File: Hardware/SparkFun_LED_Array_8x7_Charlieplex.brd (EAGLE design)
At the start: 27.9 x 43.2 mm, 73 parts

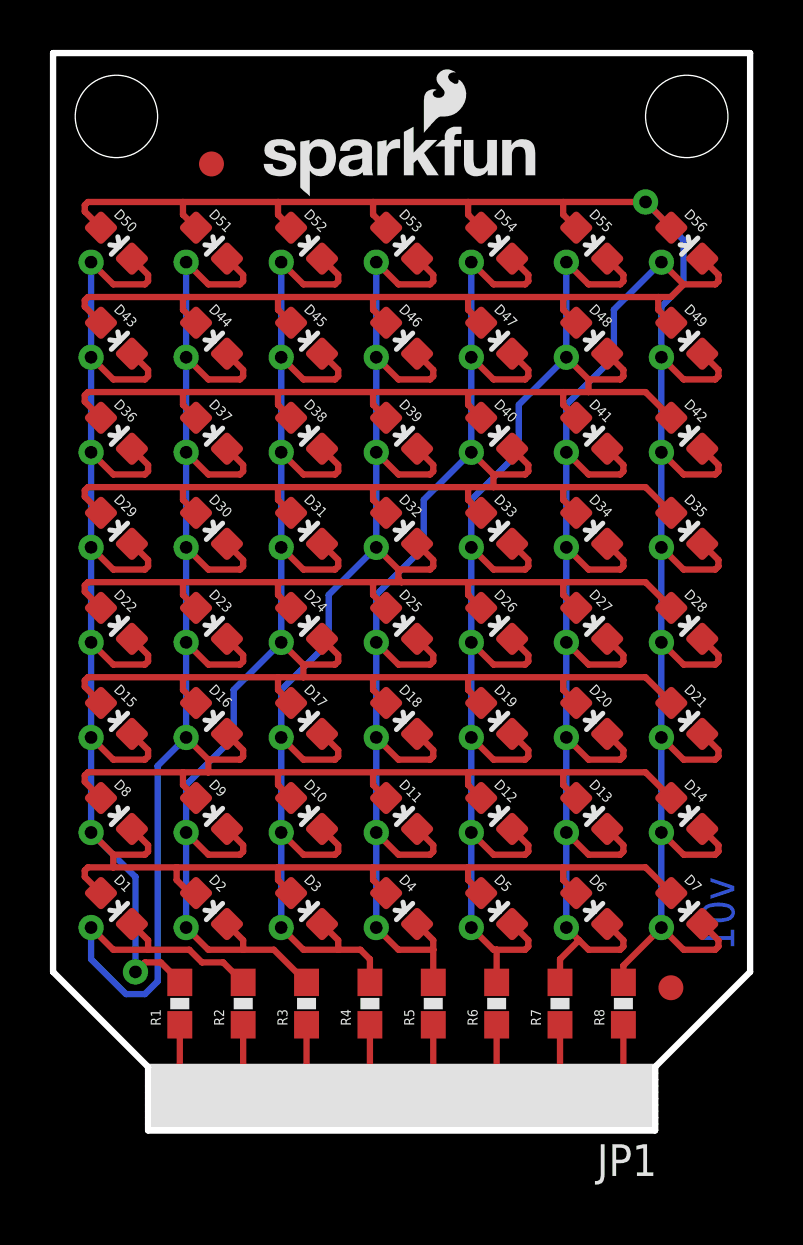
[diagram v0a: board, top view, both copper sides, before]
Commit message: Added BadgerHack logo. Moved some vias to make room.
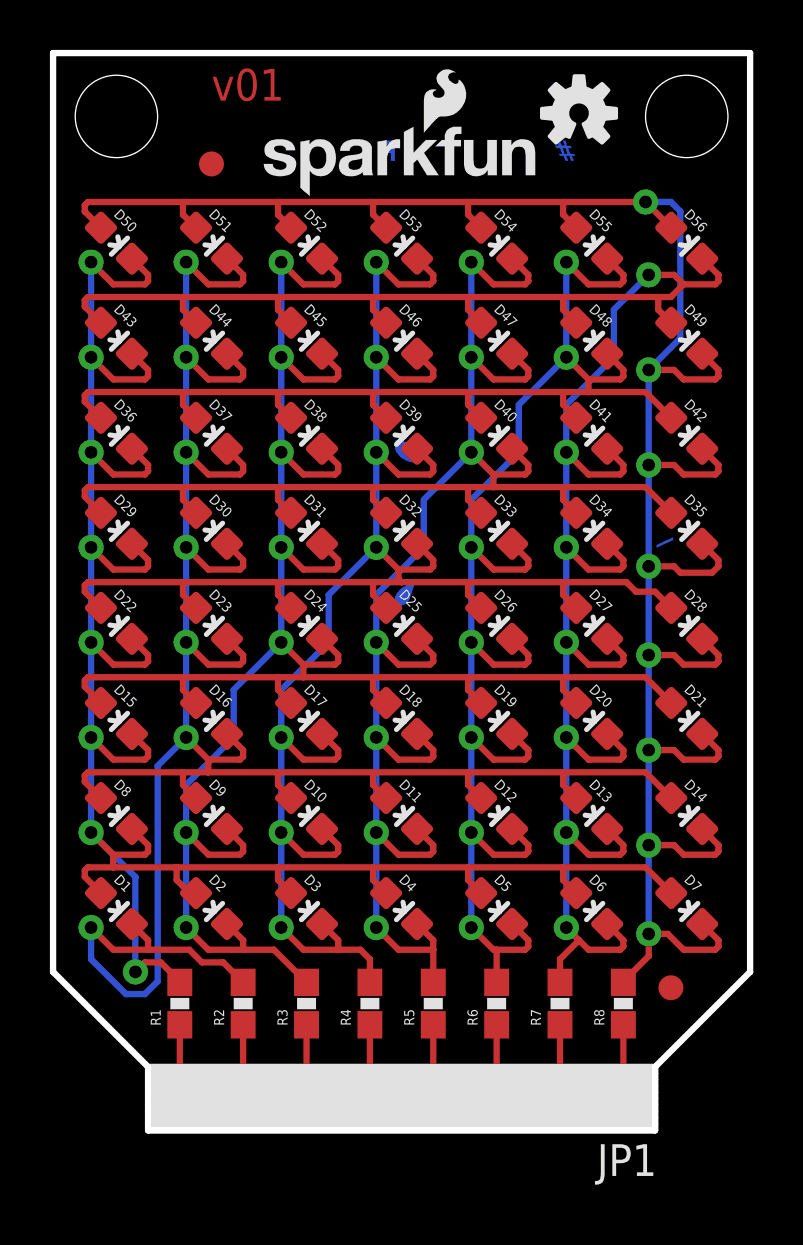
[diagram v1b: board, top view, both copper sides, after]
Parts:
- removed LOGO1: SFE_LOGO_FLAME.1_INCH, SparkFun-Aesthetics:SFE_LOGO_FLAME_.1
- added U$2: BADGERHACK_LOGO, SparkFun-Aesthetics:BADGER_HACK
- moved LOGO2 6.92 mm to (21.1, 40.8), flipped to the top, turned to 0 degrees
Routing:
- net P8: track 91.5 -> 94.1 mm
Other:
- board text removed: "sparkfun.com/badgerhack"

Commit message: Changed badger silk to separate components.
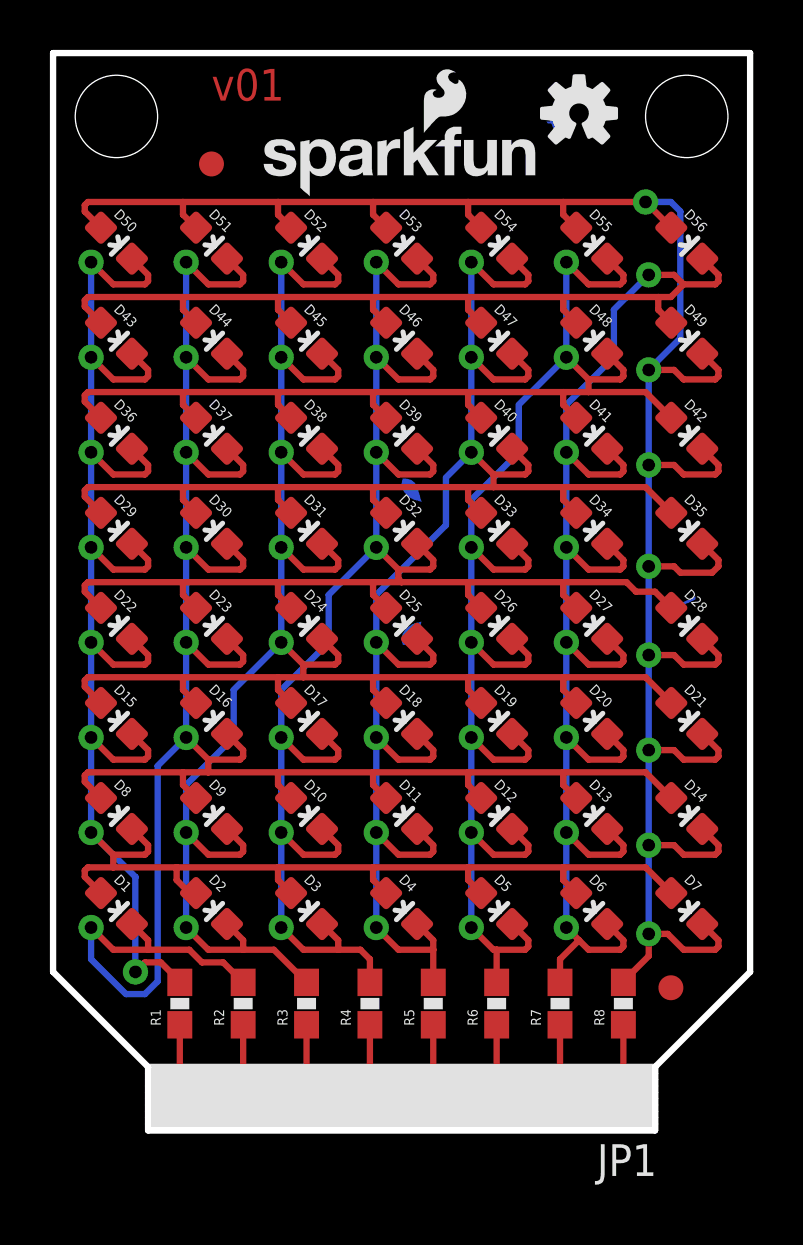
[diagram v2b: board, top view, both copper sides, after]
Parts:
- added U$3: (no value), SparkFun-Aesthetics:BADGER_ADDRESS
- added U$4: (no value), SparkFun-Aesthetics:BADGER_FACE
- added U$5: (no value), SparkFun-Aesthetics:BADGER_HASHTAG
- U$2: value BADGERHACK_LOGO -> BADGERHACK_LOGODUMMY; device SparkFun-Aesthetics:BADGER_HACK -> SparkFun-Aesthetics:DUMMY
- moved U$2 78.2 mm to (-31.8, -12.7), flipped to the top, turned to 0 degrees
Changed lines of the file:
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@@
 <element name="U$1" library="SparkFun-Aesthetics" package="SFE_LOGO_NAME_FLAME_.1" value="SFE_LOGO_NAME_FLAME.1_INCH" x="8.001" y="37.338"/>
 <element name="JP1" library="SparkFun-Connectors" package="1X08_LOCK_NO_SILK" value="" x="22.86" y="1.27" rot="R180"/>
-<element name="U$2" library="SparkFun-Aesthetics" package="BADGER_HACK" value="BADGERHACK_LOGO" x="25.4" y="40.64" rot="MR270"/>
+<element name="U$2" library="SparkFun-Aesthetics" package="DUMMY" value="BADGERHACK_LOGODUMMY" x="-31.75" y="-12.7"/>
+<element name="U$3" library="SparkFun-Aesthetics" package="BADGER_ADDRESS" value="" x="25.781" y="34.417" rot="MR270"/>
+<element name="U$4" library="SparkFun-Aesthetics" package="BADGER_FACE" value="" x="21.59" y="29.972" rot="MR270"/>
+<element name="U$5" library="SparkFun-Aesthetics" package="BADGER_HASHTAG" value="" x="20.447" y="40.132" rot="MR0"/>
 </elements>
 <signals>
@@
 <wire x1="15.24" y1="7.239" x2="15.24" y2="7.62" width="0.254" layer="1"/>
 <wire x1="13.843" y1="7.239" x2="15.24" y2="7.239" width="0.254" layer="1"/>
-<wire x1="12.954" y1="21.463" x2="14.859" y2="23.368" width="0.254" layer="16"/>
-<wire x1="14.859" y1="23.368" x2="14.859" y2="25.273" width="0.254" layer="16"/>
-<wire x1="14.859" y1="25.273" x2="16.764" y2="27.178" width="0.254" layer="16"/>
+<wire x1="12.954" y1="21.463" x2="15.748" y2="24.257" width="0.254" layer="16"/>
 <wire x1="12.954" y1="19.558" x2="12.954" y2="15.748" width="0.254" layer="16"/>
 <wire x1="12.954" y1="21.463" x2="12.954" y2="19.558" width="0.254" layer="16"/>
+<wire x1="15.748" y1="24.257" x2="15.748" y2="26.162" width="0.254" layer="16"/>
+<wire x1="15.748" y1="26.162" x2="16.764" y2="27.178" width="0.254" layer="16"/>
 </signal>
 <signal name="P1">

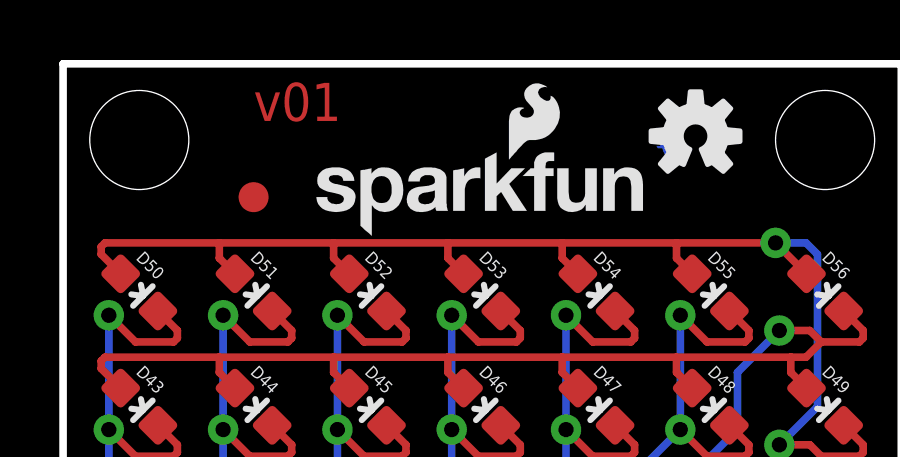
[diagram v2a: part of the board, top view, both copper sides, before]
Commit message: Updated hash logo to fix invalid polygon error.
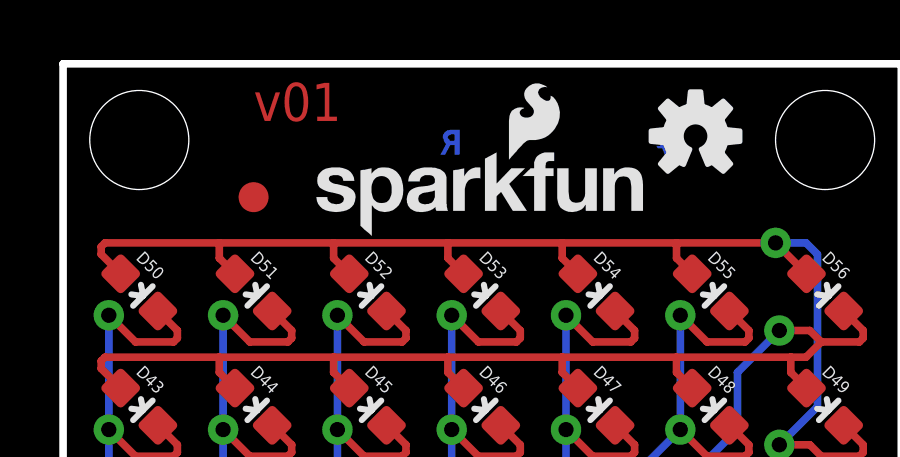
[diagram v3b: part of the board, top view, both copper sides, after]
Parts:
- renumbered U$5 to U$6
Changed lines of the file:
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@@
 <setting verticaltext="up"/>
 </settings>
-<grid distance="0.01" unitdist="inch" unit="inch" style="dots" multiple="1" display="yes" altdistance="0.005" altunitdist="inch" altunit="inch"/>
+<grid distance="0.05" unitdist="inch" unit="inch" style="dots" multiple="1" display="yes" altdistance="0.005" altunitdist="inch" altunit="inch"/>
 <layers>
-<layer number="1" name="Top" color="4" fill="1" visible="no" active="yes"/>
+<layer number="1" name="Top" color="4" fill="1" visible="yes" active="yes"/>
 <layer number="2" name="Route2" color="1" fill="3" visible="no" active="yes"/>
 <layer number="15" name="Route15" color="4" fill="6" visible="no" active="yes"/>
@@
 <layer number="19" name="Unrouted" color="6" fill="1" visible="yes" active="yes"/>
 <layer number="20" name="Dimension" color="15" fill="1" visible="yes" active="yes"/>
-<layer number="21" name="tPlace" color="16" fill="1" visible="no" active="yes"/>
+<layer number="21" name="tPlace" color="16" fill="1" visible="yes" active="yes"/>
 <layer number="22" name="bPlace" color="14" fill="1" visible="yes" active="yes"/>
-<layer number="23" name="tOrigins" color="15" fill="1" visible="no" active="yes"/>
+<layer number="23" name="tOrigins" color="15" fill="1" visible="yes" active="yes"/>
 <layer number="24" name="bOrigins" color="15" fill="1" visible="yes" active="yes"/>
 <layer number="25" name="tNames" color="7" fill="1" visible="no" active="yes"/>
@@
 <layer number="43" name="vRestrict" color="2" fill="10" visible="no" active="yes"/>
 <layer number="44" name="Drills" color="7" fill="1" visible="no" active="yes"/>
-<layer number="45" name="Holes" color="7" fill="1" visible="no" active="yes"/>
+<layer number="45" name="Holes" color="7" fill="1" visible="yes" active="yes"/>
 <layer number="46" name="Milling" color="3" fill="1" visible="no" active="yes"/>
-<layer number="51" name="tDocu" color="6" fill="1" visible="no" active="yes"/>
+<layer number="51" name="tDocu" color="6" fill="1" visible="yes" active="yes"/>
 <layer number="52" name="bDocu" color="7" fill="1" visible="no" active="yes"/>
 <layer number="3" name="Route3" color="4" fill="3" visible="no" active="no"/>
@@
 <element name="U$3" library="SparkFun-Aesthetics" package="BADGER_ADDRESS" value="" x="25.781" y="34.417" rot="MR270"/>
 <element name="U$4" library="SparkFun-Aesthetics" package="BADGER_FACE" value="" x="21.59" y="29.972" rot="MR270"/>
-<element name="U$5" library="SparkFun-Aesthetics" package="BADGER_HASHTAG" value="" x="20.447" y="40.132" rot="MR0"/>
+<element name="U$6" library="SparkFun-Aesthetics" package="BADGER_HASHTAG" value="" x="20.447" y="40.132" rot="MR0"/>
 </elements>
 <signals>

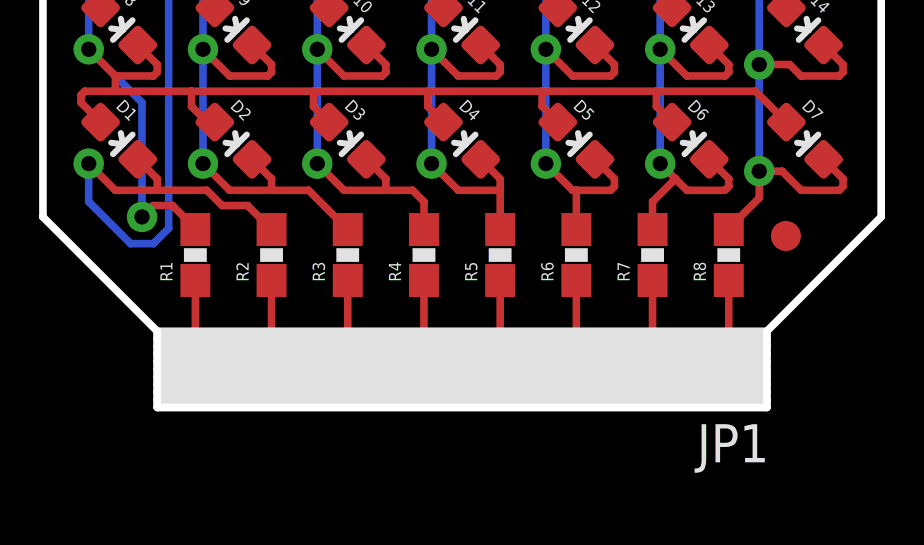
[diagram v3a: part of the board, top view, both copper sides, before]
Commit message: Fixed changes from QC checklist. Added dimensions and pin numbers in silk on top.
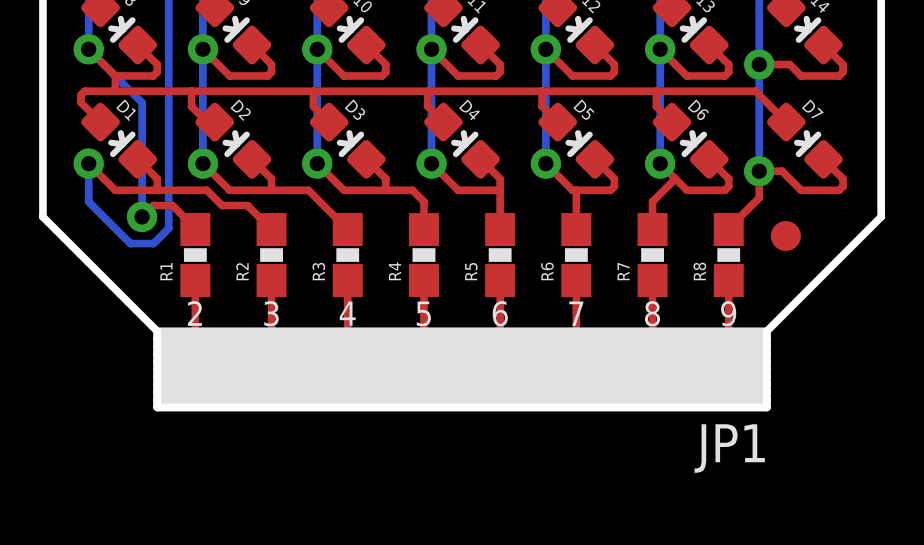
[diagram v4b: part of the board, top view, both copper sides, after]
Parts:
- moved FRAME1 15.2 mm to (-11.4, -26.7)
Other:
- board text added: "0.13"
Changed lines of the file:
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@@
 <setting verticaltext="up"/>
 </settings>
-<grid distance="0.05" unitdist="inch" unit="inch" style="dots" multiple="1" display="yes" altdistance="0.005" altunitdist="inch" altunit="inch"/>
+<grid distance="0.1" unitdist="inch" unit="inch" style="dots" multiple="1" display="yes" altdistance="0.05" altunitdist="inch" altunit="inch"/>
 <layers>
 <layer number="1" name="Top" color="4" fill="1" visible="yes" active="yes"/>
@@
 <layer number="45" name="Holes" color="7" fill="1" visible="yes" active="yes"/>
 <layer number="46" name="Milling" color="3" fill="1" visible="no" active="yes"/>
+<layer number="47" name="Measures" color="7" fill="1" visible="yes" active="yes"/>
 <layer number="51" name="tDocu" color="6" fill="1" visible="yes" active="yes"/>
 <layer number="52" name="bDocu" color="7" fill="1" visible="no" active="yes"/>
@@
 <layer number="37" name="tTest" color="7" fill="1" visible="no" active="no"/>
 <layer number="38" name="bTest" color="7" fill="1" visible="no" active="no"/>
-<layer number="47" name="Measures" color="7" fill="1" visible="no" active="no"/>
 <layer number="48" name="Document" color="7" fill="1" visible="no" active="no"/>
 <layer number="49" name="Reference" color="7" fill="1" visible="no" active="no"/>
@@
 <wire x1="27.305" y1="6.985" x2="0.635" y2="6.985" width="0.254" layer="51"/>
 <wire x1="0.635" y1="6.985" x2="0.635" y2="37.465" width="0.254" layer="51"/>
+<dimension x1="0" y1="0" x2="3.81" y2="0" x3="1.905" y3="-3.81" textsize="1.778" textratio="15" layer="47" dtype="horizontal" unit="inch"/>
+<dimension x1="0" y1="0" x2="24.13" y2="0" x3="12.065" y3="-7.62" textsize="1.778" textratio="15" layer="47" dtype="horizontal" unit="inch"/>
+<dimension x1="0" y1="0" x2="27.94" y2="6.35" x3="13.97" y3="-11.43" textsize="1.778" textratio="15" layer="47" dtype="horizontal" unit="inch"/>
+<dimension x1="0" y1="0" x2="3.81" y2="2.54" x3="-10.16" y3="1.27" textsize="1.778" textratio="15" layer="47" dtype="vertical" unit="inch"/>
+<dimension x1="0" y1="0" x2="0" y2="6.35" x3="-6.35" y3="3.175" textsize="1.778" textratio="15" layer="47" dtype="vertical" unit="inch"/>
+<dimension x1="0" y1="0" x2="0" y2="43.18" x3="-19.05" y3="21.59" textsize="1.778" textratio="15" layer="47" dtype="vertical" unit="inch"/>
+<dimension x1="0" y1="0" x2="2.54" y2="40.64" x3="-15.24" y3="20.32" textsize="1.778" textratio="15" layer="47" dtype="vertical" unit="inch"/>
+<dimension x1="0" y1="43.18" x2="2.54" y2="40.64" x3="1.27" y3="48.26" textsize="1.778" textratio="15" layer="47" dtype="horizontal" unit="inch"/>
+<dimension x1="3.7084" y1="41.8084" x2="7.62" y2="45.72" x3="8.89" y3="45.72" textsize="1.778" textratio="15" layer="47" dtype="leader" unit="inch"/>
+<text x="9.525" y="45.72" size="1.778" layer="47" ratio="15" align="center-left">0.13</text>
+<text x="5.08" y="2.7178" size="0.8128" layer="21" font="vector" ratio="15" align="bottom-center">2</text>
+<text x="7.62" y="2.7178" size="0.8128" layer="21" font="vector" ratio="15" align="bottom-center">3</text>
+<text x="10.16" y="2.7178" size="0.8128" layer="21" font="vector" ratio="15" align="bottom-center">4</text>
+<text x="12.7" y="2.7178" size="0.8128" layer="21" font="vector" ratio="15" align="bottom-center">5</text>
+<text x="15.24" y="2.7178" size="0.8128" layer="21" font="vector" ratio="15" align="bottom-center">6</text>
+<text x="17.78" y="2.7178" size="0.8128" layer="21" font="vector" ratio="15" align="bottom-center">7</text>
+<text x="20.32" y="2.7178" size="0.8128" layer="21" font="vector" ratio="15" align="bottom-center">8</text>
+<text x="22.86" y="2.7178" size="0.8128" layer="21" font="vector" ratio="15" align="bottom-center">9</text>
 </plain>
 <attributes>
@@
 <element name="FID1" library="SparkFun-Aesthetics" package="FIDUCIAL-1X2" value="FIDUCIAL1X2" x="24.765" y="5.715"/>
 <element name="FID2" library="SparkFun-Aesthetics" package="FIDUCIAL-1X2" value="FIDUCIAL1X2" x="6.35" y="38.735"/>
-<element name="FRAME1" library="SparkFun-Aesthetics" package="CREATIVE_COMMONS" value="" x="-11.43" y="-11.43" smashed="yes">
+<element name="FRAME1" library="SparkFun-Aesthetics" package="CREATIVE_COMMONS" value="" x="-11.43" y="-26.67" smashed="yes">
 <attribute name="VERSION" value="v01" x="6.35" y="41.275" size="1.27" layer="1" font="vector" ratio="15" rot="SR0"/>
-<attribute name="DESIGNER" value="Shawn Hymel" x="15.24" y="-11.43" size="1.778" layer="51"/>
+<attribute name="DESIGNER" value="Shawn Hymel" x="15.24" y="-26.67" size="1.778" layer="51"/>
 </element>
 <element name="LOGO2" library="SparkFun-Aesthetics" package="OSHW-LOGO-S" value="OSHW-LOGOS" x="21.082" y="40.767"/>
